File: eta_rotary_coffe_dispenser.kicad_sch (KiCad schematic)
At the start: 54 parts, among them J1 Conn_01x08, J3 AVR-ISP-6, J4 Conn_01x02, J5 Conn_01x04, J6 Conn_01x02, J7 Conn_01x02, Q1 IRF640NPbF, Q2 IRF640NPbF, Q3 CPH3350-TL-W, SW1 SW_Push, U1 ATmega328P-A, U2 L7805, Y1 Crystal

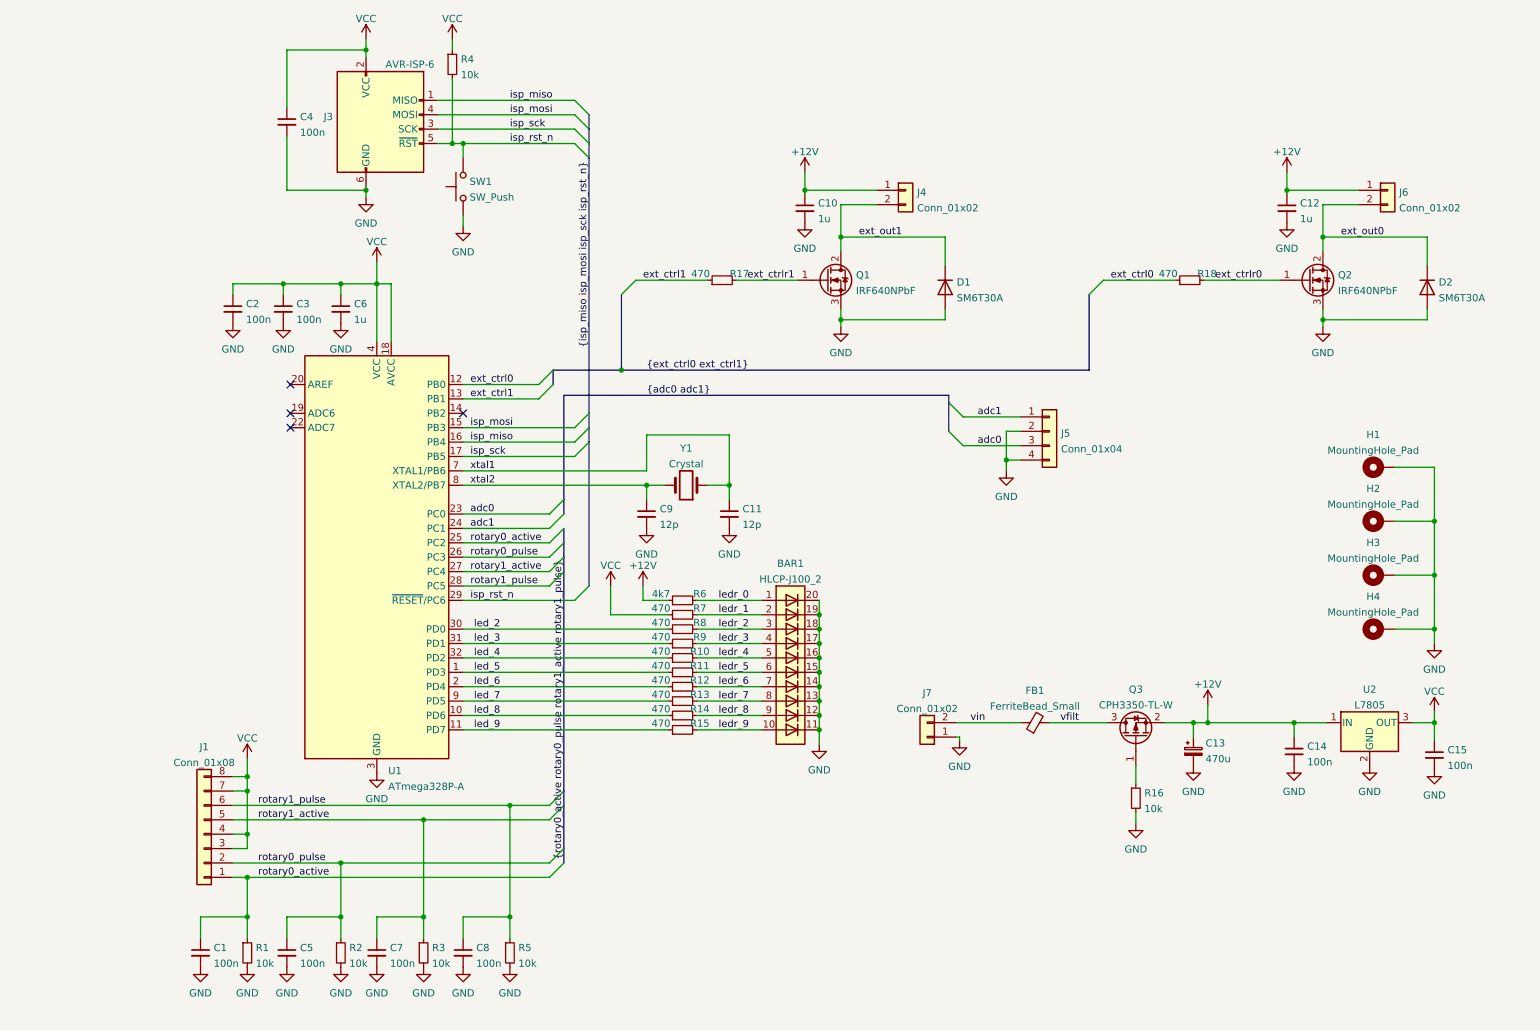
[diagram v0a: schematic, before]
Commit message: start rev 2 op project with can and weight sens
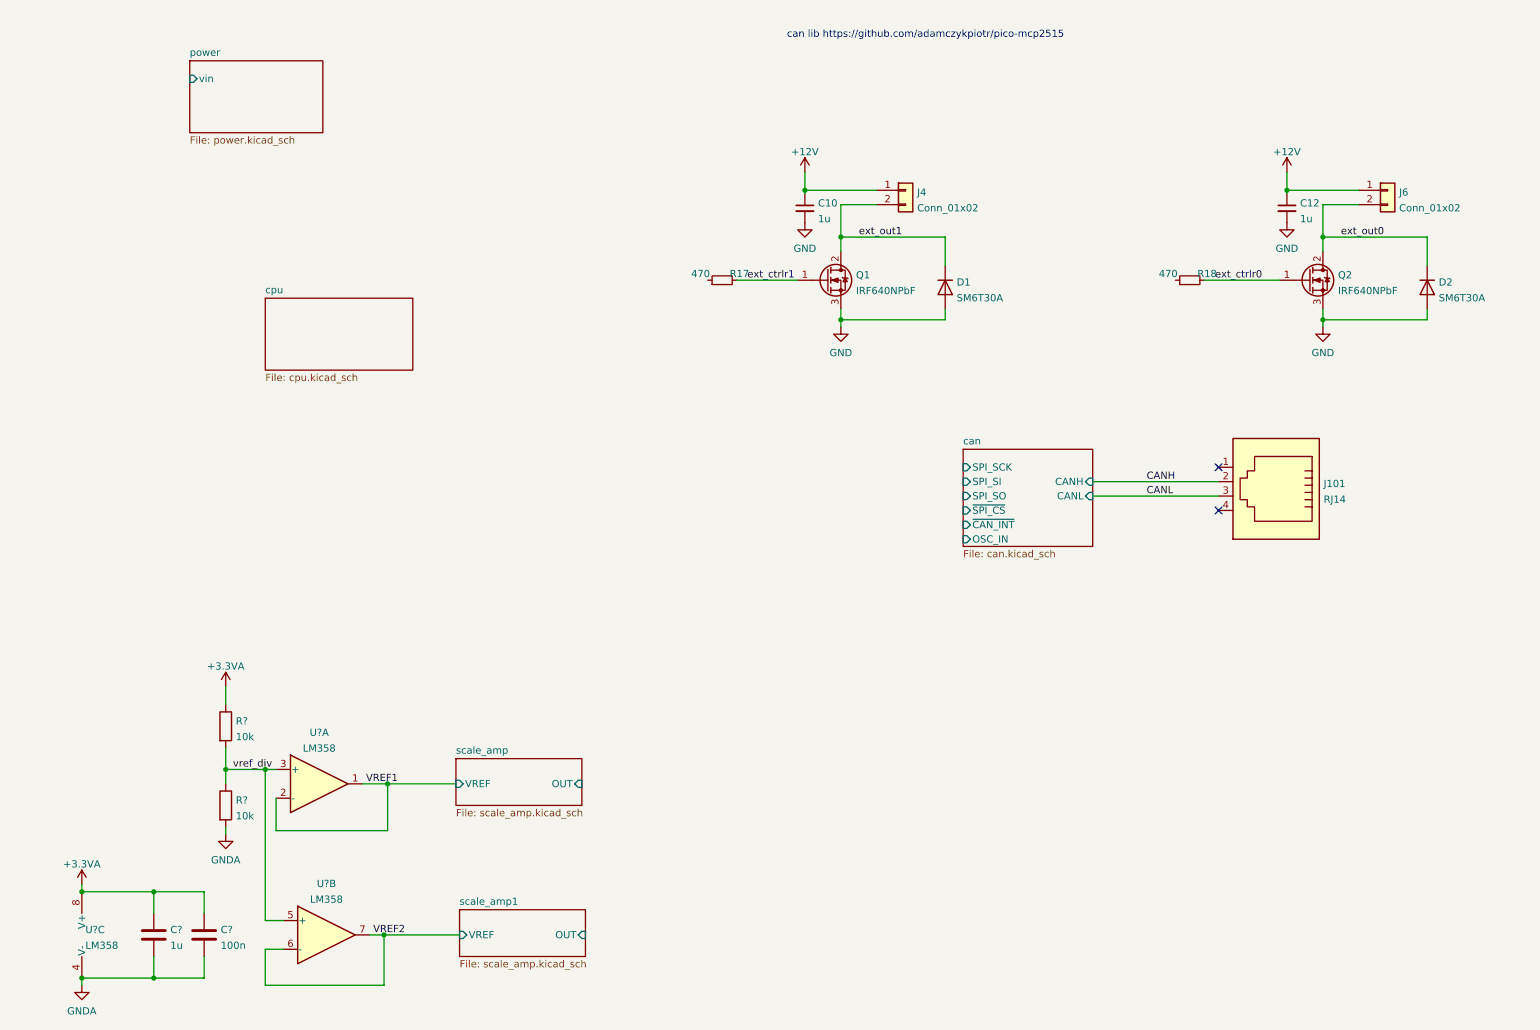
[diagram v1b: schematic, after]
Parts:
- removed BAR1: HLCP-J100_2, Display:HLCP-J100, symbol LED:HLCP-J100_2
- removed C1, C14, C15, C2, C3, C4, C5, C7, C8: 100n, Resistor_SMD:R_0603_1608Metric_Pad0.98x0.95mm_HandSolder, symbol Device:C_Small
- removed C11, C9: 12p, Resistor_SMD:R_0603_1608Metric_Pad0.98x0.95mm_HandSolder, symbol Device:C_Small
- removed C13: 470u, Capacitor_SMD:CP_Elec_10x10.5, symbol Device:C_Polarized_Small
- removed C6: 1u, Resistor_SMD:R_0603_1608Metric_Pad0.98x0.95mm_HandSolder, symbol Device:C_Small
- removed FB1: FerriteBead_Small, Resistor_SMD:R_0603_1608Metric_Pad0.98x0.95mm_HandSolder, symbol Device:FerriteBead_Small
- removed H1, H2, H3, H4: MountingHole_Pad, MountingHole:MountingHole_3.2mm_M3_DIN965_Pad, symbol Mechanical:MountingHole_Pad
- removed J1: Conn_01x08, TerminalBlock_Phoenix:TerminalBlock_Phoenix_MKDS-1,5-8-5.08_1x08_P5.08mm_Horizontal, symbol Connector_Generic:Conn_01x08
- removed J3: AVR-ISP-6, Connector_PinHeader_2.54mm:PinHeader_2x03_P2.54mm_Vertical, symbol Connector:AVR-ISP-6
- removed J5: Conn_01x04, TerminalBlock_Phoenix:TerminalBlock_Phoenix_MKDS-1,5-4_1x04_P5.00mm_Horizontal, symbol Connector_Generic:Conn_01x04
- removed J7: Conn_01x02, TerminalBlock:TerminalBlock_Altech_AK300-2_P5.00mm, symbol Connector_Generic:Conn_01x02
- removed Q3: CPH3350-TL-W, Package_TO_SOT_SMD:SOT-23_Handsoldering, symbol Device:Q_PMOS_GSD
- removed R1, R16, R2, R3, R4, R5: 10k, Resistor_SMD:R_0603_1608Metric_Pad0.98x0.95mm_HandSolder, symbol Device:R_Small
- removed R10, R11, R12, R13, R14, R15, R7, R8, R9: 470, Resistor_SMD:R_0603_1608Metric_Pad0.98x0.95mm_HandSolder, symbol Device:R_Small
- removed R6: 4k7, Resistor_SMD:R_0603_1608Metric_Pad0.98x0.95mm_HandSolder, symbol Device:R_Small
- removed SW1: SW_Push, good_things:push_sw_purple, symbol Switch:SW_Push
- removed U1: ATmega328P-A, Package_QFP:TQFP-32_7x7mm_P0.8mm, symbol MCU_Microchip_ATmega:ATmega328P-A
- removed U2: L7805, Package_TO_SOT_THT:TO-220-3_Vertical, symbol Regulator_Linear:L7805
- removed Y1: Crystal, Crystal:Crystal_SMD_EuroQuartz_MQ2-2Pin_7.0x5.0mm_HandSoldering, symbol Device:Crystal
- added C?: 100n, Capacitor_SMD:C_0603_1608Metric_Pad1.08x0.95mm_HandSolder, symbol Device:C
- added C?: 1u, Capacitor_SMD:C_0603_1608Metric_Pad1.08x0.95mm_HandSolder, symbol Device:C
- added J101: RJ14, symbol Connector:RJ14
- added R? (x2): 10k, Resistor_SMD:R_0603_1608Metric_Pad0.98x0.95mm_HandSolder, symbol Device:R
- added U?: LM358, Package_SO:SO-8_3.9x4.9mm_P1.27mm, symbol Amplifier_Operational:LM358
- added U? (x2): LM358, symbol Amplifier_Operational:LM358
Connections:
- net ext_ctrl0: no longer names the net of R18.1
- net ext_ctrl1: no longer names the net of R17.1
- new net +3.3VA: C?.1, C?.1, R?.1, U?.8 (V+)
- new net CANH: J101.2
- new net CANL: J101.3
- new net GNDA: C?.2, C?.2, R?.2, U?.4 (V-)
- new net VREF1: U?.1, U?.2 (-)
- new net VREF2: U?.6 (-), U?.7
- new net vref_div: R?.1, R?.2, U?.3 (+), U?.5 (+)
- no-connect marks 4 -> 2
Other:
- added sheet can (can.kicad_sch)
- added sheet cpu (cpu.kicad_sch)
- added sheet power (power.kicad_sch)
- added sheet scale_amp (scale_amp.kicad_sch)
- added sheet scale_amp1 (scale_amp.kicad_sch)
- note added: "can lib https://github.com/adamczykpiotr/pico-mcp2515"

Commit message: some form of schematic done, still lots to test
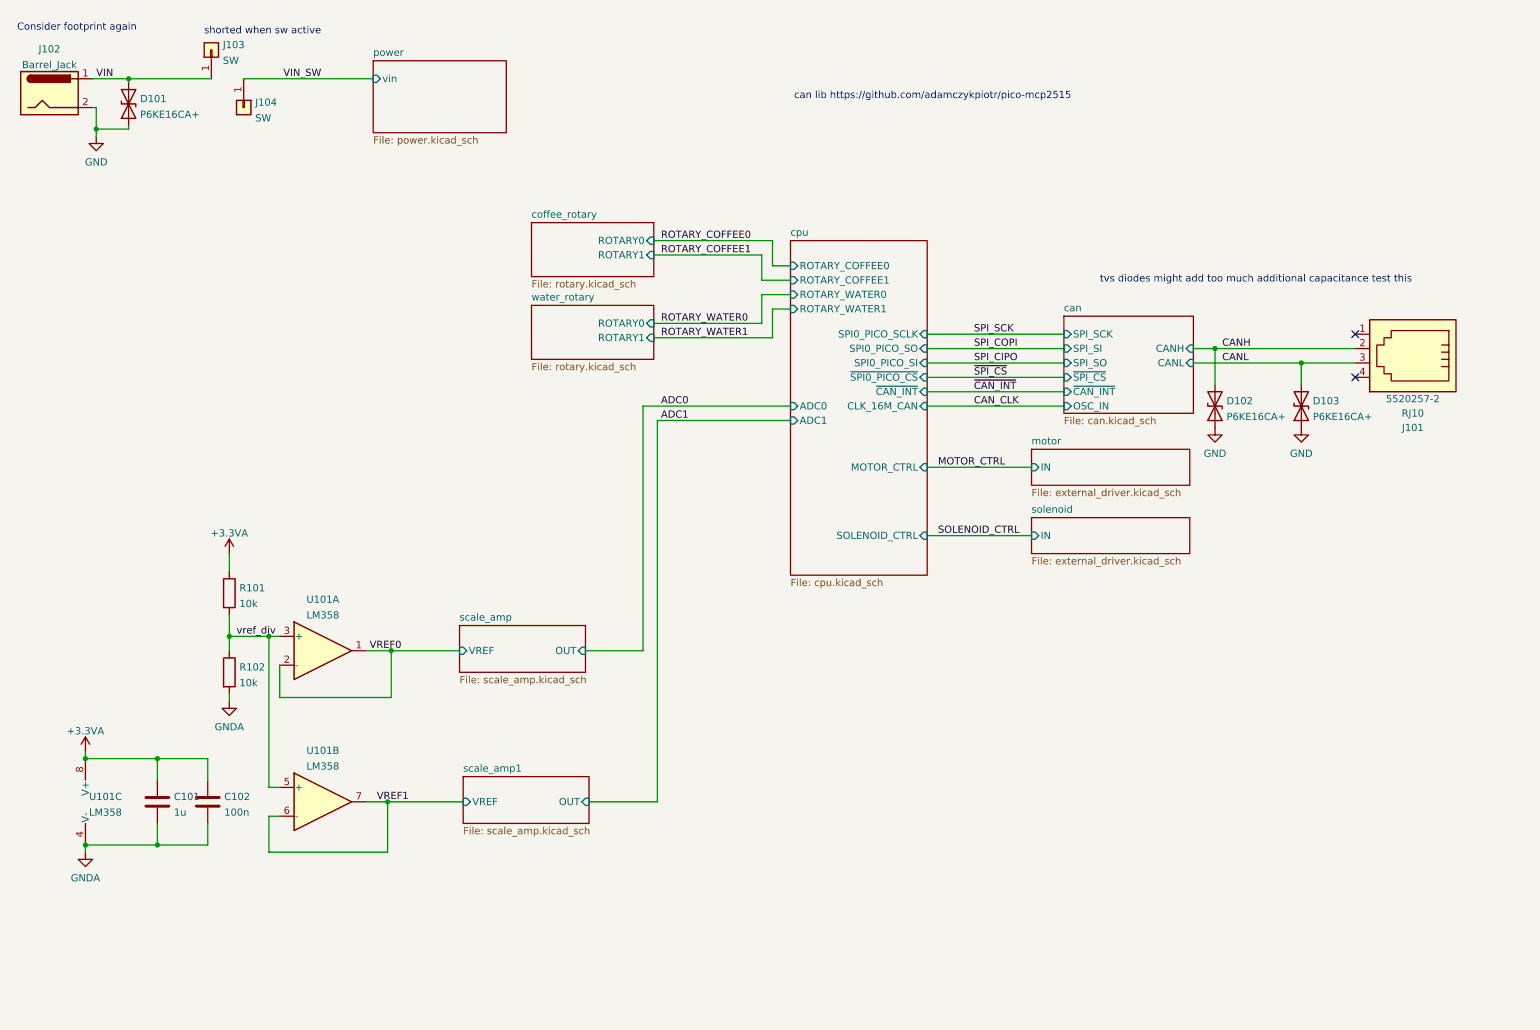
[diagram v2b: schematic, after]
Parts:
- removed C10, C12: 1u, Resistor_SMD:R_0603_1608Metric_Pad0.98x0.95mm_HandSolder, symbol Device:C_Small
- removed D1, D2: SM6T30A, Diode_SMD:D_SMB, symbol Device:D
- removed J101: RJ14, symbol Connector:RJ14
- removed J4, J6: Conn_01x02, TerminalBlock:TerminalBlock_Altech_AK300-2_P5.00mm, symbol Connector_Generic:Conn_01x02
- removed Q1, Q2: IRF640NPbF, Package_TO_SOT_SMD:TO-263-2, symbol Device:Q_NMOS_GDS
- removed R17, R18: 470, Resistor_SMD:R_0603_1608Metric_Pad0.98x0.95mm_HandSolder, symbol Device:R_Small
- added D101, D102, D103: P6KE16CA+, Diode_THT:D_DO-15_P2.54mm_Vertical_AnodeUp, symbol Device:D_TVS
- added J101: RJ10, CAN-Distributor:TE_5520257-2, symbol Connector:RJ10
- added J102: Barrel_Jack, Connector_BarrelJack:BarrelJack_CUI_PJ-063AH_Horizontal_CircularHoles, symbol Connector:Barrel_Jack
- added J103, J104: SW, good_things:TE_726386-2, symbol Connector_Generic:Conn_01x01
- gave numbers to parts that had none: 5
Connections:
- net VREF2 is gone; now on net VREF1: U101.6 (-), U101.7
- net CANH: now also D102.2 (A2), J101.2
- net CANL: now also D103.2 (A2), J101.3
- net GND: now also D101.1 (A1), D102.1 (A1), D103.1 (A1), J102.2
- net VREF1: no longer U101.1, U101.2 (-)
- new net VIN: D101.2 (A2), J102.1, J103.1 (Pin_1)
- new net VIN_SW: J104.1 (Pin_1)
- new net VREF0: U101.1, U101.2 (-)
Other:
- added sheet coffee_rotary (rotary.kicad_sch)
- added sheet motor (external_driver.kicad_sch)
- added sheet solenoid (external_driver.kicad_sch)
- added sheet water_rotary (rotary.kicad_sch)
- sheet cpu ports: added ADC0, ADC1, CLK_16M_CAN, MOTOR_CTRL, ROTARY_COFFEE0, ROTARY_COFFEE1, ROTARY_WATER0, ROTARY_WATER1, SOLENOID_CTRL, SPI0_PICO_SCLK, SPI0_PICO_SI, SPI0_PICO_SO, ~{CAN_INT}, ~{SPI0_PICO_CS}; removed none
- note added: "Consider footprint again"
- note added: "shorted when sw active"
- note added: "tvs diodes might add too much additional capacitance test this"
- moved on the sheet: C101, C102, R101, R102, U101A, U101B, U101C
